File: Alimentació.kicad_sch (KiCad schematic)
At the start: 26 parts, among them J1 USB_C_Receptacle_PowerOnly_6P, U2 BQ25628ERYKR, U3 TLV61048DBVR, U4 TLV61070ADBV

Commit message: actualitzar ultrima versio pcb/esquematic
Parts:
- removed BT1: Battery, symbol Device:Battery
- removed U3: TLV61048DBVR, SOT-23-6_DBV_TEX, symbol TLV61048:TLV61048DBVR
- added C14: 100 n, Capacitor_SMD:C_0201_0603Metric, symbol Device:C
- added C15, C18: 22 n, Capacitor_SMD:C_0201_0603Metric, symbol Device:C
- added C16: 10 u, Capacitor_SMD:C_0201_0603Metric, symbol Device:C
- added C17: 22 u, Capacitor_SMD:C_0201_0603Metric, symbol Device:C
- added C19: 4,7 u, Capacitor_SMD:C_0201_0603Metric, symbol Device:C
- added C20: 100 u, Capacitor_SMD:C_0201_0603Metric, symbol Device:C
- added J7: Conn_01x02_Socket, Connector_JST:JST_PH_B2B-PH-K_1x02_P2.00mm_Vertical, symbol Connector:Conn_01x02_Socket
- added L3: 900 n, Inductor_SMD:L_1008_2520Metric_Pad1.43x2.20mm_HandSolder, symbol Device:L
- added Q1: QM6015D, Package_TO_SOT_SMD:TO-252-2, symbol Transistor_FET:QM6015D
- added R15: 86,6 k, Resistor_SMD:R_0201_0603Metric, symbol Device:R
- added R16: 56,2 k, Resistor_SMD:R_0201_0603Metric, symbol Device:R
- added R17: 274 k, Resistor_SMD:R_0201_0603Metric, symbol Device:R
- added R18: 178 k, Resistor_SMD:R_0201_0603Metric, symbol Device:R
- added R19: 732 k, Resistor_SMD:R_0201_0603Metric, symbol Device:R
- added R20: 80,6 k, Mounting_Wuerth:Mounting_Wuerth_WA-SMSE-ExternalM3_H6mm_9771060360, symbol Device:R
- added U3: TPS611781RNWR, RNW0013A, symbol TPS61178:TPS611781RNWR
- C8, C9: footprint (none) -> Capacitor_SMD:C_0201_0603Metric
- D1, D2: footprint (none) -> Diode_SMD:D_0201_0603Metric
- J1: footprint (none) -> USBC_6_DEALON:USB_C_6_DEALON
- L1, L2: footprint (none) -> Inductor_SMD:L_1008_2520Metric_Pad1.43x2.20mm_HandSolder
- R1: value 1200 -> 1,2 k; footprint (none) -> Resistor_SMD:R_0201_0603Metric
- R2, R3, R4, R5, R6, R7, TH1: footprint (none) -> Resistor_SMD:R_0201_0603Metric
- U2: footprint WQFN-HR18__RYK_TEX -> BQ25628E:WQFN-HR18__RYK_TEX
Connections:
- net GND: now also C16.2, C17.2, C18.2, C19.2, C20.2, J7.2 (Pin_2), R16.2, R17.2, R20.2, U3.2 (AGND), U3.6 (PGND)
- net at C6.1, U2.8 (BAT): now also J7.1 (Pin_1)
- new net: C19.1, U3.10 (VCC)
- new net: R17.1, U3.1 (FREQ_SYNC)
- new net: C14.2, U3.13 (BST)
- new net: R16.1, U3.3 (ILIMIT)
- new net: R15.1, U3.4 (COMP)
- new net: R19.2, R20.1, U3.5 (FB)
- new net: C14.1, L3.2, U3.7 (SW)
- new net: C15.1, C16.1, Q1.2 (D), R18.1, U3.8 (VOUT)
- new net: C15.2, Q1.1 (G), R18.2, U3.9 (DISDRV)
- new net: C18.1, R15.2
- new net +12V: C17.1, Q1.3 (S), R19.1
- new net vsys: C20.1, L3.1, U3.11 (EN), U3.12 (VIN)
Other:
- moved on the sheet: C1, C2, C3, C4, C5, C6, C7, C8, C9, D1, D2, J1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

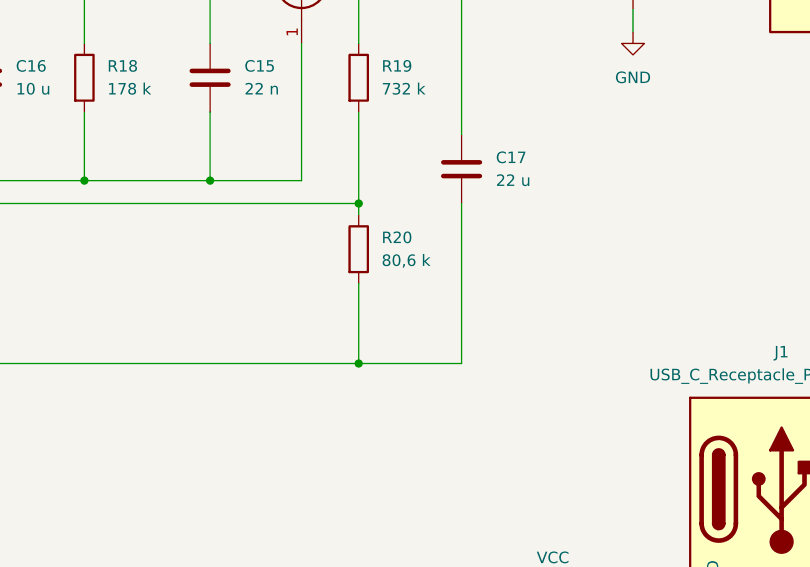
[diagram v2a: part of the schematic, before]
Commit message: arreclat footprints/symbol
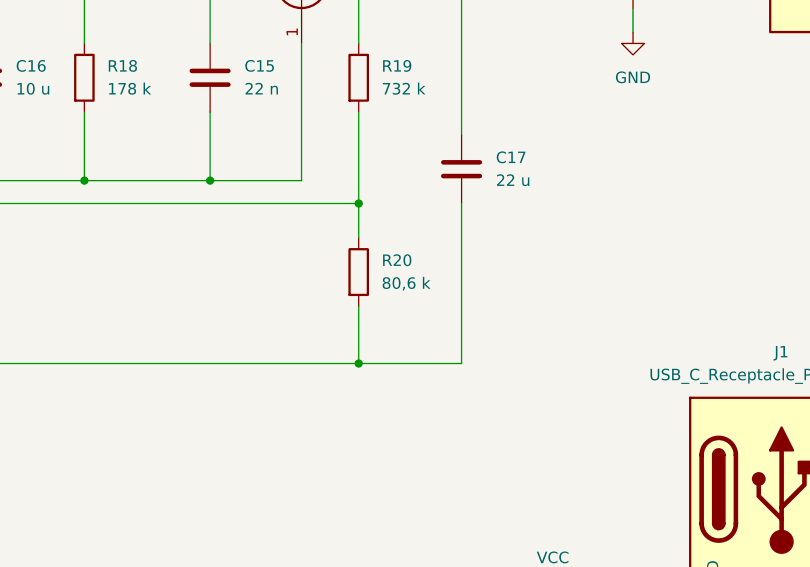
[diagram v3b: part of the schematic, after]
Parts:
- R20: footprint Mounting_Wuerth:Mounting_Wuerth_WA-SMSE-ExternalM3_H6mm_9771060360 -> Resistor_SMD:R_0603_1608Metric
- U3: footprint RNW0013A -> tps611781rnwr:RNW0013A
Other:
- moved on the sheet: R20
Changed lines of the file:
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@@
 	)
 	(junction
-		(at 177.8 106.68)
-		(diameter 0)
-		(color 0 0 0 0)
-	)
-	(junction
 		(at 177.8 63.5)
 		(diameter 0)
@@
 	)
 	(junction
+		(at 177.8 106.68)
+		(diameter 0)
+		(color 0 0 0 0)
+	)
+	(junction
 		(at 114.3 146.05)
 		(diameter 0)
@@
 	(wire
 		(pts
-			(xy 189.23 106.68) (xy 177.8 106.68)
-		)
-		(stroke
-			(width 0)
-			(type default)
-		)
-	)
-	(wire
-		(pts
 			(xy 39.37 168.91) (xy 39.37 172.72)
 		)
@@
 	(wire
 		(pts
-			(xy 177.8 88.9) (xy 177.8 90.17)
+			(xy 177.8 88.9) (xy 177.8 92.71)
 		)
 		(stroke
@@
 	(wire
 		(pts
-			(xy 177.8 97.79) (xy 177.8 106.68)
+			(xy 177.8 100.33) (xy 177.8 106.68)
 		)
 		(stroke
@@
 	(wire
 		(pts
+			(xy 177.8 106.68) (xy 189.23 106.68)
+		)
+		(stroke
+			(width 0)
+			(type default)
+		)
+	)
+	(wire
+		(pts
 			(xy 67.31 146.05) (xy 46.99 146.05)
 		)
@@
 			)
 		)
-		(property "Footprint" "RNW0013A"
+		(property "Footprint" "tps611781rnwr:RNW0013A"
 			(at 101.6 68.58 0)
 			(effects
@@
 	(symbol
 		(lib_id "Device:R")
-		(at 177.8 93.98 0)
+		(at 177.8 96.52 0)
 		(unit 1)
 		(exclude_from_sim no)
@@
 		(dnp no)
 		(property "Reference" "R20"
-			(at 180.34 92.7099 0)
+			(at 180.34 95.2499 0)
 			(effects
 				(font
@@
 		)
 		(property "Value" "80,6 k"
-			(at 180.34 95.2499 0)
+			(at 180.34 97.7899 0)
 			(effects
 				(font
@@
 			)
 		)
-		(property "Footprint" "Mounting_Wuerth:Mounting_Wuerth_WA-SMSE-ExternalM3_H6mm_9771060360"
-			(at 176.022 93.98 90)
+		(property "Footprint" "Resistor_SMD:R_0603_1608Metric"
+			(at 176.022 96.52 90)
 			(effects
 				(font
@@
 		)
 		(property "Datasheet" "~"
-			(at 177.8 93.98 0)
+			(at 177.8 96.52 0)
 			(effects
 				(font
@@
 		)
 		(property "Description" "Resistor"
-			(at 177.8 93.98 0)
+			(at 177.8 96.52 0)
 			(effects
 				(font

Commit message: esquematic fet v1
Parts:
- C14, C15, C16, C17, C18, C19, C20, C8, C9: footprint Capacitor_SMD:C_0201_0603Metric -> Capacitor_SMD:C_0603_1608Metric_Pad1.08x0.95mm_HandSolder
- R1, R15, R16, R17, R18, R19, R2, R3, R4, R5, R6, R7: footprint Resistor_SMD:R_0201_0603Metric -> Resistor_SMD:R_0603_1608Metric
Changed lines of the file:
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@@
 			)
 		)
-		(property "Footprint" "Resistor_SMD:R_0201_0603Metric"
+		(property "Footprint" "Resistor_SMD:R_0603_1608Metric"
 			(at 249.682 78.74 90)
 			(effects
@@
 			)
 		)
-		(property "Footprint" "Resistor_SMD:R_0201_0603Metric"
+		(property "Footprint" "Resistor_SMD:R_0603_1608Metric"
 			(at 259.588 137.16 90)
 			(effects
@@
 			)
 		)
-		(property "Footprint" "Capacitor_SMD:C_0201_0603Metric"
+		(property "Footprint" "Capacitor_SMD:C_0603_1608Metric_Pad1.08x0.95mm_HandSolder"
 			(at 42.8752 85.09 0)
 			(effects
@@
 			)
 		)
-		(property "Footprint" "Resistor_SMD:R_0201_0603Metric"
+		(property "Footprint" "Resistor_SMD:R_0603_1608Metric"
 			(at 145.542 74.93 90)
 			(effects
@@
 			)
 		)
-		(property "Footprint" "Resistor_SMD:R_0201_0603Metric"
+		(property "Footprint" "Resistor_SMD:R_0603_1608Metric"
 			(at 55.88 145.288 90)
 			(effects
@@
 			)
 		)
-		(property "Footprint" "Resistor_SMD:R_0201_0603Metric"
+		(property "Footprint" "Resistor_SMD:R_0603_1608Metric"
 			(at 61.722 91.44 90)
 			(effects
@@
 			)
 		)
-		(property "Footprint" "Capacitor_SMD:C_0201_0603Metric"
+		(property "Footprint" "Capacitor_SMD:C_0603_1608Metric_Pad1.08x0.95mm_HandSolder"
 			(at 75.8952 104.14 0)
 			(effects
@@
 			)
 		)
-		(property "Footprint" "Resistor_SMD:R_0201_0603Metric"
+		(property "Footprint" "Resistor_SMD:R_0603_1608Metric"
 			(at 249.682 66.04 90)
 			(effects
@@
 			)
 		)
-		(property "Footprint" "Resistor_SMD:R_0201_0603Metric"
+		(property "Footprint" "Resistor_SMD:R_0603_1608Metric"
 			(at 51.562 91.44 90)
 			(effects
@@
 			)
 		)
-		(property "Footprint" "Capacitor_SMD:C_0201_0603Metric"
+		(property "Footprint" "Capacitor_SMD:C_0603_1608Metric_Pad1.08x0.95mm_HandSolder"
 			(at 30.1752 85.09 0)
 			(effects
@@
 			)
 		)
-		(property "Footprint" "Capacitor_SMD:C_0201_0603Metric"
+		(property "Footprint" "Capacitor_SMD:C_0603_1608Metric_Pad1.08x0.95mm_HandSolder"
 			(at 209.2452 67.31 0)
 			(effects
@@
 			)
 		)
-		(property "Footprint" "Resistor_SMD:R_0201_0603Metric"
+		(property "Footprint" "Resistor_SMD:R_0603_1608Metric"
 			(at 73.152 91.44 90)
 			(effects
@@
 			)
 		)
-		(property "Footprint" "Capacitor_SMD:C_0201_0603Metric"
+		(property "Footprint" "Capacitor_SMD:C_0603_1608Metric_Pad1.08x0.95mm_HandSolder"
 			(at 136.8552 78.74 0)
 			(effects
@@
 			)
 		)
-		(property "Footprint" "Resistor_SMD:R_0201_0603Metric"
+		(property "Footprint" "Resistor_SMD:R_0603_1608Metric"
 			(at 246.888 137.16 90)
 			(effects
@@
 			)
 		)
-		(property "Footprint" "Capacitor_SMD:C_0201_0603Metric"
+		(property "Footprint" "Capacitor_SMD:C_0603_1608Metric_Pad1.08x0.95mm_HandSolder"
 			(at 129.2352 55.88 0)
 			(effects
@@
 			)
 		)
-		(property "Footprint" "Resistor_SMD:R_0201_0603Metric"
+		(property "Footprint" "Resistor_SMD:R_0603_1608Metric"
 			(at 176.022 74.93 90)
 			(effects
@@
 			)
 		)
-		(property "Footprint" "Capacitor_SMD:C_0201_0603Metric"
+		(property "Footprint" "Capacitor_SMD:C_0603_1608Metric_Pad1.08x0.95mm_HandSolder"
 			(at 162.2552 78.74 0)
 			(effects
@@
 			)
 		)
-		(property "Footprint" "Resistor_SMD:R_0201_0603Metric"
+		(property "Footprint" "Resistor_SMD:R_0603_1608Metric"
 			(at 37.592 165.1 90)
 			(effects
@@
 			)
 		)
-		(property "Footprint" "Capacitor_SMD:C_0201_0603Metric"
+		(property "Footprint" "Capacitor_SMD:C_0603_1608Metric_Pad1.08x0.95mm_HandSolder"
 			(at 265.1252 71.12 0)
 			(effects
@@
 			)
 		)
-		(property "Footprint" "Resistor_SMD:R_0201_0603Metric"
+		(property "Footprint" "Resistor_SMD:R_0603_1608Metric"
 			(at 37.592 177.8 90)
 			(effects
@@
 			)
 		)
-		(property "Footprint" "Capacitor_SMD:C_0201_0603Metric"
+		(property "Footprint" "Capacitor_SMD:C_0603_1608Metric_Pad1.08x0.95mm_HandSolder"
 			(at 190.1952 88.9 0)
 			(effects

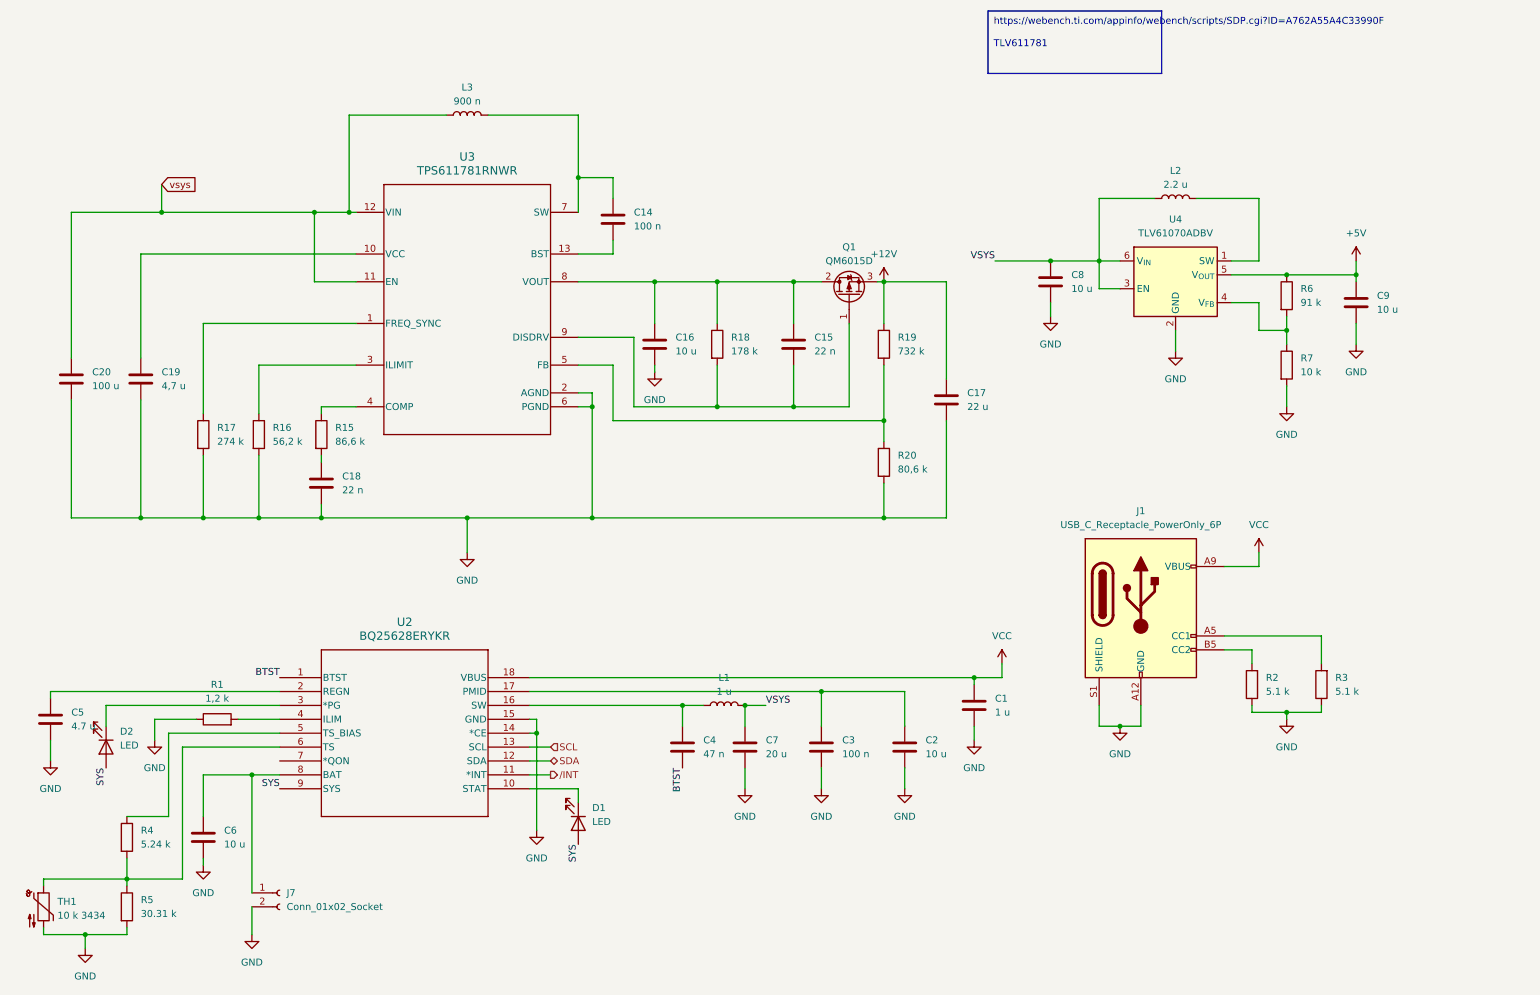
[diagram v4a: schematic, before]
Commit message: Col·locats tots els components
S'han col·locat tots els components a la seva posició a la placa a més d'haver-ne afegit algun més.
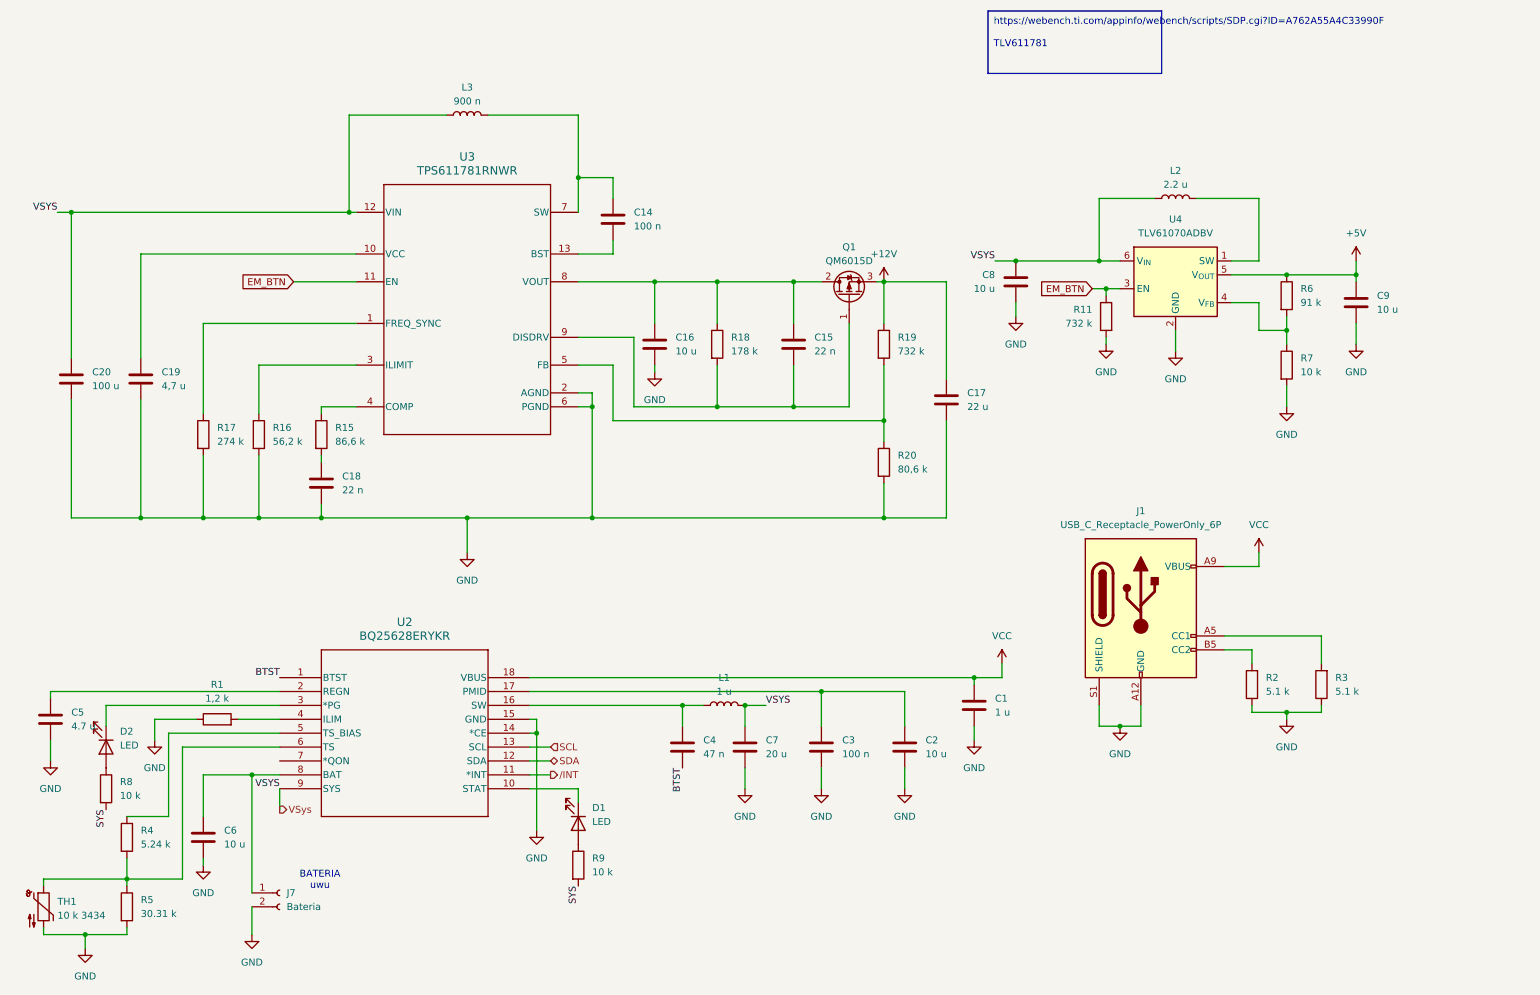
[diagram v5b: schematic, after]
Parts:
- added R11: 732 k, Resistor_SMD:R_0603_1608Metric, symbol Device:R
- added R8, R9: 10 k, Resistor_SMD:R_0603_1608Metric, symbol Device:R
- D1, D2: footprint Diode_SMD:D_0201_0603Metric -> Diode_SMD:D_0603_1608Metric
- J7: value Conn_01x02_Socket -> Bateria
- TH1: footprint Resistor_SMD:R_0201_0603Metric -> Resistor_SMD:R_0603_1608Metric_Pad0.98x0.95mm_HandSolder
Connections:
- net GND: now also R11.2
- net SYS: now also R8.2, R9.2; no longer D1.2 (A), D2.2 (A), U2.9 (SYS)
- net VSYS renamed VSys
- net VSys: now also C20.1, L3.1, U2.9 (SYS), U3.12 (VIN); no longer U4.3 (EN)
- removed net vsys: C20.1, L3.1, U3.11 (EN), U3.12 (VIN)
- new net: D2.2 (A), R8.1
- new net: D1.2 (A), R9.1
- new net EM_BTN: R11.1, U3.11 (EN), U4.3 (EN)
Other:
- note added: "BATERIA uwu"
- moved on the sheet: C8

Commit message: Revisio de la placa
S'ha revisat la placa
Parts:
- added D5, D6: 5 V, Diode_SMD:D_SOD-323, symbol Device:D_Zener
- added D9: 12 V, Diode_SMD:D_SOD-323, symbol Device:D_Zener
- added J14: Conn_01x02_Pin, Connector_JST:JST_PH_B2B-PH-K_1x02_P2.00mm_Vertical, symbol Connector:Conn_01x02_Pin
- J7: footprint Connector_JST:JST_PH_B2B-PH-K_1x02_P2.00mm_Vertical -> Connector_AMASS:AMASS_XT30U-M_1x02_P5.0mm_Vertical
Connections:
- net SYS is gone; now on net VSys: R8.2, R9.2
- net +12V: now also D9.1 (K)
- net +5V: now also D6.1 (K)
- net GND: now also J7.1 (Pin_1), D5.2 (A), D6.2 (A), D9.2 (A), J14.1 (Pin_1); no longer J7.2 (Pin_2)
- net VCC: now also D5.1 (K), J14.2 (Pin_2)
- net at C6.1, U2.8 (BAT): now also J7.2 (Pin_2); no longer J7.1 (Pin_1)
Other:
- note added: "Càrrega QI"

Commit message: Actualitzats valors dels components
S'han actualitzat els valors de components d'acord als comprats, s'ha canviat algun valor per conveniència, i s'ha acabat de donar valors a tots els components
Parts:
- C20: value 100 u -> 22 u
- C7: value 20 u -> 22 u
- D5, D6: value 5 V -> DESD5V0S1BA-7
- D9: value 12 V -> SD12-7
- J7: value Bateria -> XT-30 male
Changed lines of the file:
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@@
 	(label "VSYS"
 		(at 198.12 59.69 180)
-		(fields_autoplaced yes)
 		(effects
 			(font
@@
 	(label "VSYS"
 		(at 156.21 140.97 0)
-		(fields_autoplaced yes)
 		(effects
 			(font
@@
 	(label "VSYS"
 		(at 121.92 173.99 270)
-		(fields_autoplaced yes)
 		(effects
 			(font
@@
 	(label "BTST"
 		(at 140.97 152.4 270)
-		(fields_autoplaced yes)
 		(effects
 			(font
@@
 	(label "VSYS"
 		(at 67.31 156.21 180)
-		(fields_autoplaced yes)
 		(effects
 			(font
@@
 	(label "VSYS"
 		(at 35.56 160.02 270)
-		(fields_autoplaced yes)
 		(effects
 			(font
@@
 	(label "BTST"
 		(at 67.31 135.89 180)
-		(fields_autoplaced yes)
 		(effects
 			(font
@@
 	(label "VSYS"
 		(at 26.67 50.8 180)
-		(fields_autoplaced yes)
 		(effects
 			(font
@@
 		(shape input)
 		(at 116.84 148.59 0)
-		(fields_autoplaced yes)
 		(effects
 			(font
@@
 		(shape output)
 		(at 67.31 160.02 0)
-		(fields_autoplaced yes)
 		(effects
 			(font
@@
 		(shape bidirectional)
 		(at 116.84 151.13 0)
-		(fields_autoplaced yes)
 		(effects
 			(font
@@
 		(shape output)
 		(at 116.84 153.67 0)
-		(fields_autoplaced yes)
 		(effects
 			(font
@@
 			)
 		)
-		(property "Value" "12 V"
+		(property "Value" "SD12-7"
 			(at 191.77 43.1799 90)
 			(effects
@@
 			)
 		)
-		(property "Value" "5 V"
+		(property "Value" "DESD5V0S1BA-7"
 			(at 278.13 68.5799 90)
 			(effects
@@
 			)
 		)
-		(property "Value" "20 u"
+		(property "Value" "22 u"
 			(at 156.21 149.8599 0)
 			(effects
@@
 			)
 		)
-		(property "Value" "100 u"
+		(property "Value" "22 u"
 			(at 33.02 82.5499 0)
 			(effects
@@
 			)
 		)
-		(property "Value" "Bateria"
+		(property "Value" "XT-30 male"
 			(at 68.58 175.2601 0)
 			(effects
@@
 			)
 		)
-		(property "Value" "5 V"
+		(property "Value" "DESD5V0S1BA-7"
 			(at 248.92 120.6499 90)
 			(effects
